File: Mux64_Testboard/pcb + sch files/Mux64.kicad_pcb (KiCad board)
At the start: 4 copper layers, 201.3 x 130.3 mm, 125 parts, among them J1 QTE-020-01-X-D-A, J10 Conn_01x24, J11 Screw_Terminal_01x12, J12 Screw_Terminal_01x06, J13 Screw_Terminal_01x12, J14 Screw_Terminal_01x12, J16 Screw_Terminal_01x12, J17 Screw_Terminal_01x12, J18 Screw_Terminal_01x12, J2 QTE-020-01-X-D-A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

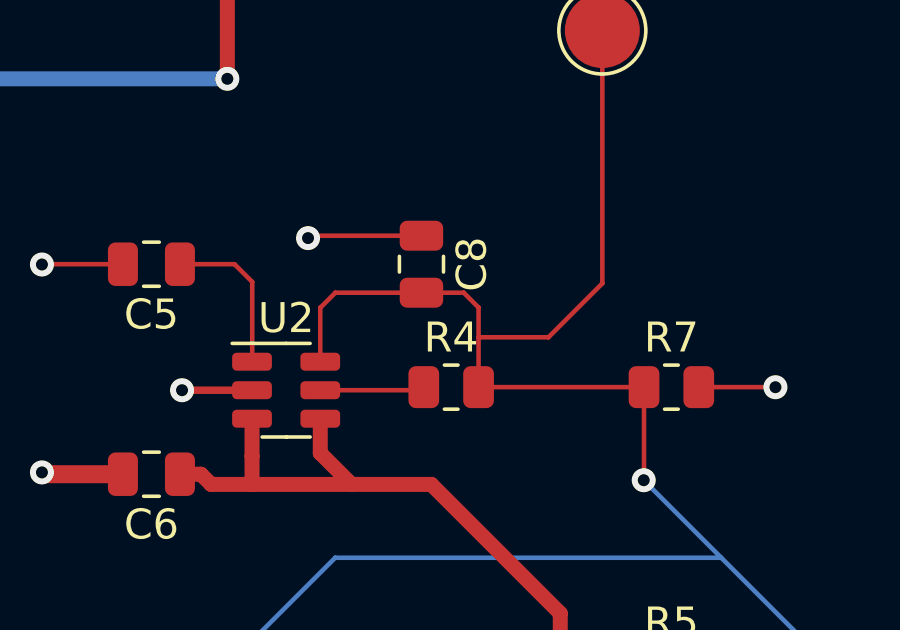
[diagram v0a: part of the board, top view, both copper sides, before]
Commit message: Added images of physical board changes
physical changes from batch order from version 1v0
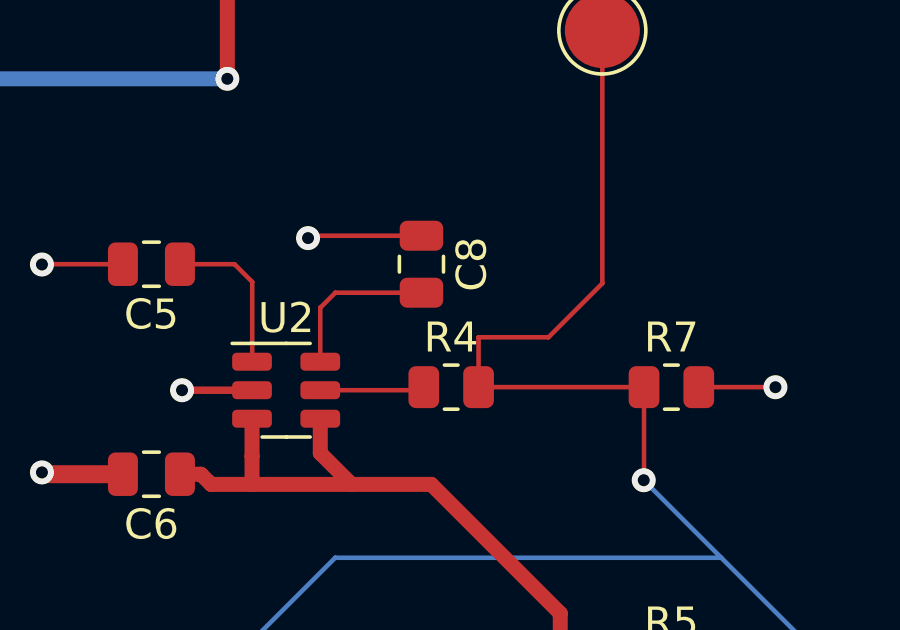
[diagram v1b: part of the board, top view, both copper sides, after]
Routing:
- net B_a4: track 135.9 -> 132.8 mm
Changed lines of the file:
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@@
   (segment (start 186.2239 59.1561) (end 188.5539 59.1561) (width 0.1524) (layer "F.Cu") (net 5))
   (segment (start 188.5539 59.1561) (end 190.35 57.36) (width 0.1524) (layer "F.Cu") (net 5))
-  (segment (start 184.32 57.67) (end 185.73 57.67) (width 0.1524) (layer "F.Cu") (net 5))
-  (segment (start 185.73 57.67) (end 186.2239 58.1639) (width 0.1524) (layer "F.Cu") (net 5))
   (segment (start 231.59 87.29) (end 217.03 72.73) (width 0.1524) (layer "F.Cu") (net 5))
   (segment (start 186.2239 59.1561) (end 186.2239 60.8174) (width 0.1524) (layer "F.Cu") (net 5))
   (segment (start 184.32 57.67) (end 181.45 57.67) (width 0.1524) (layer "F.Cu") (net 5))
-  (segment (start 186.2239 58.1639) (end 186.2239 59.1561) (width 0.1524) (layer "F.Cu") (net 5))
   (segment (start 181.45 57.67) (end 180.9475 58.1725) (width 0.1524) (layer "F.Cu") (net 5))
   (segment (start 237.86 89.63) (end 233.93 89.63) (width 0.1524) (layer "F.Cu") (net 5))

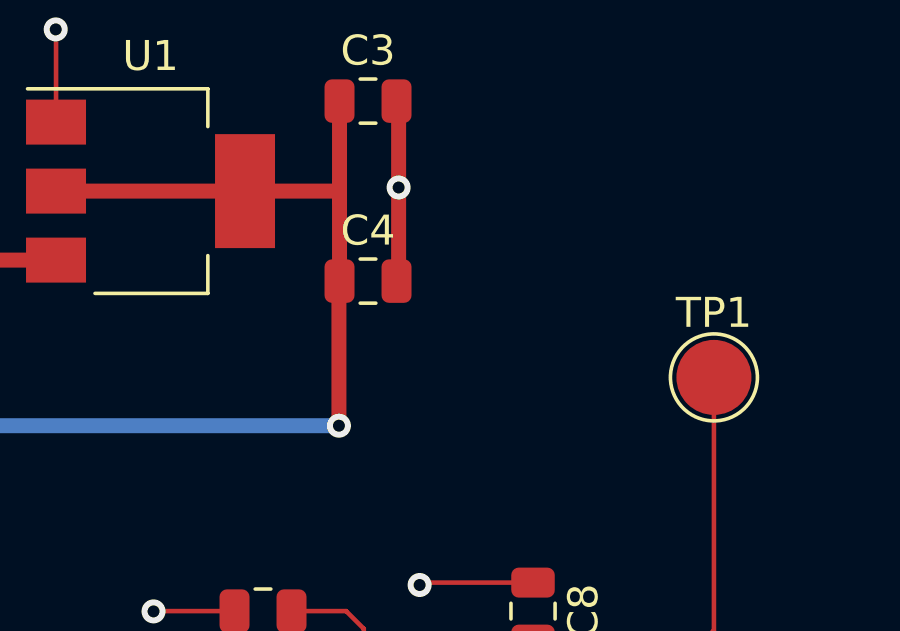
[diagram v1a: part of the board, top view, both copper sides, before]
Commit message: Made improvements on v1.0
Added a 100Ohm load to voltage regulator. Fixed wiring with voltage reference
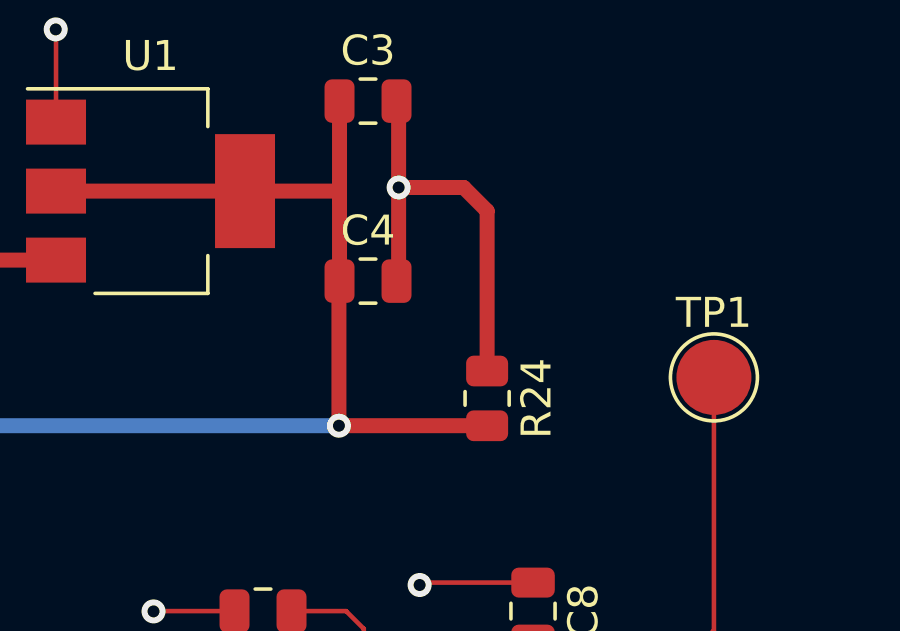
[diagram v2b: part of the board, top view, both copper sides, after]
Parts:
- added R24: 1Kohm, Resistor_SMD:R_0805_2012Metric, F.Cu at (182.8, 49.6)
- C1, C3: value 100nF -> 0.1uF
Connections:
- C8 pad 2: B_a4 -> Net-(R4-Pad1)
- U2 pad 6: B_a4 -> Net-(R4-Pad1)
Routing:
- net MUX64_A11: track 486.3 -> 494.9 mm
- net Net-(R4-Pad1): track 3.49 -> 8.87 mm
- net B_a4: track 132.8 -> 127.4 mm
- net 1.2V: track 138.5 -> 143.4 mm
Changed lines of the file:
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@@
       (effects (font (size 1 1) (thickness 0.15)))
     )
-    (fp_text value "100nF" (at 0 1.68) (layer "F.Fab")
+    (fp_text value "0.1uF" (at 0 1.68) (layer "F.Fab")
       (effects (font (size 1 1) (thickness 0.15)))
     )
@@
       (net 218 "Net-(R4-Pad1)") (pinfunction "OUTS") (pintype "input"))
     (pad "6" smd roundrect (at 1.1375 -0.95) (size 1.325 0.6) (layers "F.Cu" "F.Paste" "F.Mask") (roundrect_rratio 0.25)
-      (net 5 "B_a4") (pinfunction "OUTF") (pintype "input"))
+      (net 218 "Net-(R4-Pad1)") (pinfunction "OUTF") (pintype "input"))
     (model "${KICAD6_3DMODEL_DIR}/Package_TO_SOT_SMD.3dshapes/SOT-23-6.wrl"
       (offset (xyz 0 0 0))
@@
       (effects (font (size 1 1) (thickness 0.15)))
     )
-    (fp_text value "100nF" (at 0 1.68) (layer "F.Fab")
+    (fp_text value "0.1uF" (at 0 1.68) (layer "F.Fab")
       (effects (font (size 1 1) (thickness 0.15)))
     )
@@
       (net 185 "MUX64_A11") (pintype "passive"))
     (pad "2" smd roundrect (at 0.95 0 270) (size 1 1.45) (layers "F.Cu" "F.Paste" "F.Mask") (roundrect_rratio 0.25)
-      (net 5 "B_a4") (pintype "passive"))
+      (net 218 "Net-(R4-Pad1)") (pintype "passive"))
     (model "${KICAD6_3DMODEL_DIR}/Capacitor_SMD.3dshapes/C_0805_2012Metric.wrl"
       (offset (xyz 0 0 0))
@@
   )
   (footprint "Resistor_SMD:R_0805_2012Metric" (layer "F.Cu")
+    (at 182.79 49.63 -90)
+    (descr "Resistor SMD 0805 (2012 Metric), square (rectangular) end terminal, IPC_7351 nominal, (Body size source: IPC-SM-782 page 72, https://www.pcb-3d.com/wordpress/wp-content/uploads/ipc-sm-782a_amendment_1_and_2.pdf), generated with kicad-footprint-generator")
+    (tags "resistor")
+    (property "Sheetfile" "mux64-regulators.kicad_sch")
+    (property "Sheetname" "mux64-regulators")
+    (attr smd)
+    (fp_text reference "R24" (at 0 -1.65 90) (layer "F.SilkS")
+      (effects (font (size 1 1) (thickness 0.15)))
+    )
+    (fp_text value "1Kohm" (at 0 1.65 90) (layer "F.Fab")
+      (effects (font (size 1 1) (thickness 0.15)))
+    )
+    (fp_text user "${REFERENCE}" (at 0 0 90) (layer "F.Fab")
+      (effects (font (size 0.5 0.5) (thickness 0.08)))
+    )
+    (fp_line (start -0.227064 -0.735) (end 0.227064 -0.735) (layer "F.SilkS") (width 0.12))
+    (fp_line (start -0.227064 0.735) (end 0.227064 0.735) (layer "F.SilkS") (width 0.12))
+    (fp_line (start 1.68 0.95) (end -1.68 0.95) (layer "F.CrtYd") (width 0.05))
+    (fp_line (start -1.68 -0.95) (end 1.68 -0.95) (layer "F.CrtYd") (width 0.05))
+    (fp_line (start 1.68 -0.95) (end 1.68 0.95) (layer "F.CrtYd") (width 0.05))
+    (fp_line (start -1.68 0.95) (end -1.68 -0.95) (layer "F.CrtYd") (width 0.05))
+    (fp_line (start 1 0.625) (end -1 0.625) (layer "F.Fab") (width 0.1))
+    (fp_line (start -1 -0.625) (end 1 -0.625) (layer "F.Fab") (width 0.1))
+    (fp_line (start 1 -0.625) (end 1 0.625) (layer "F.Fab") (width 0.1))
+    (fp_line (start -1 0.625) (end -1 -0.625) (layer "F.Fab") (width 0.1))
+    (pad "1" smd roundrect (at -0.9125 0 270) (size 1.025 1.4) (layers "F.Cu" "F.Paste" "F.Mask") (roundrect_rratio 0.243902)
+      (net 185 "MUX64_A11") (pintype "passive"))
+    (pad "2" smd roundrect (at 0.9125 0 270) (size 1.025 1.4) (layers "F.Cu" "F.Paste" "F.Mask") (roundrect_rratio 0.243902)
+      (net 2 "1.2V") (pintype "passive"))
+    (model "${KICAD6_3DMODEL_DIR}/Resistor_SMD.3dshapes/R_0805_2012Metric.wrl"
+      (offset (xyz 0 0 0))
+      (scale (xyz 1 1 1))
+      (rotate (xyz 0 0 0))
+    )
+  )
+  (footprint "Resistor_SMD:R_0805_2012Metric" (layer "F.Cu")
     (at 69.14 66.74 180)
     (descr "Resistor SMD 0805 (2012 Metric), square (rectangular) end terminal, IPC_7351 nominal, (Body size source: IPC-SM-782 page 72, https://www.pcb-3d.com/wordpress/wp-content/uploads/ipc-sm-782a_amendment_1_and_2.pdf), generated with kicad-footprint-generator")
@@
   (segment (start 218.36 126.76) (end 218.36 96.47) (width 0.5) (layer "B.Cu") (net 1))
   (segment (start 177.87 42.79) (end 177.87 42.44) (width 0.5) (layer "F.Cu") (net 2))
+  (segment (start 177.85 50.54) (end 182.7875 50.54) (width 0.5) (layer "F.Cu") (net 2))
   (segment (start 148.61 100.27) (end 155.95 100.27) (width 0.5) (layer "F.Cu") (net 2))
   (segment (start 155.95 100.27) (end 155.995 100.225) (width 0.5) (layer "F.Cu") (net 2))
@@
   (segment (start 158.535 99.545) (end 158.535 96.925) (width 0.5) (layer "F.Cu") (net 2))
   (segment (start 147.2162 96.4838) (end 147.2162 98.8762) (width 0.5) (layer "F.Cu") (net 2))
+  (segment (start 182.7875 50.54) (end 182.79 50.5425) (width 0.5) (layer "F.Cu") (net 2))
   (segment (start 177.85 50.54) (end 177.85 45.74) (width 0.5) (layer "F.Cu") (net 2))
   (segment (start 153.38 91.05) (end 155.9 91.05) (width 0.5) (layer "F.Cu") (net 2))
@@
   (segment (start 231.59 87.29) (end 217.03 72.73) (width 0.1524) (layer "F.Cu") (net 5))
   (segment (start 186.2239 59.1561) (end 186.2239 60.8174) (width 0.1524) (layer "F.Cu") (net 5))
-  (segment (start 184.32 57.67) (end 181.45 57.67) (width 0.1524) (layer "F.Cu") (net 5))
-  (segment (start 181.45 57.67) (end 180.9475 58.1725) (width 0.1524) (layer "F.Cu") (net 5))
   (segment (start 237.86 89.63) (end 233.93 89.63) (width 0.1524) (layer "F.Cu") (net 5))
   (segment (start 233.93 89.63) (end 231.59 87.29) (width 0.1524) (layer "F.Cu") (net 5))
-  (segment (start 180.9475 58.1725) (end 180.9475 59.97) (width 0.1524) (layer "F.Cu") (net 5))
   (segment (start 186.2239 60.8174) (end 191.7395 60.8174) (width 0.1524) (layer "F.Cu") (net 5))
   (segment (start 191.7395 63.9105) (end 191.7395 60.8174) (width 0.1524) (layer "F.Cu") (net 5))
@@
   (segment (start 243.95 137.22) (end 246.2 137.22) (width 0.1524) (layer "F.Cu") (net 185))
   (segment (start 77.97 61.62) (end 80.26 61.62) (width 0.1524) (layer "F.Cu") (net 185))
+  (segment (start 182.79 43.38) (end 182.79 48.7175) (width 0.5) (layer "F.Cu") (net 185))
   (segment (start 111.9525 34.55) (end 114.71 34.55) (width 0.1524) (layer "F.Cu") (net 185))
   (segment (start 244 93.67) (end 246.25 93.67) (width 0.1524) (layer "F.Cu") (net 185))
@@
   (segment (start 207.82 93.67) (end 205.25 93.67) (width 0.1524) (layer "F.Cu") (net 185))
   (segment (start 243.95 132.42) (end 246.07 132.42) (width 0.1524) (layer "F.Cu") (net 185))
+  (segment (start 182.01 42.6) (end 182.79 43.38) (width 0.5) (layer "F.Cu") (net 185))
   (segment (start 210.95 43.255) (end 210.95 37.985) (width 0.1524) (layer "F.Cu") (net 185))
   (segment (start 205.82 50.03) (end 205.77 49.98) (width 0.1524) (layer "F.Cu") (net 185))
@@
   (segment (start 240.91 86.895) (end 240.91 81.625) (width 0.2) (layer "F.Cu") (net 185))
   (segment (start 244.04 52.43) (end 246.27 52.43) (width 0.1524) (layer "F.Cu") (net 185))
+  (segment (start 182.79 48.7175) (end 182.7675 48.7175) (width 0.25) (layer "F.Cu") (net 185))
   (segment (start 240.95 54.875) (end 240.95 58.02) (width 0.1524) (layer "F.Cu") (net 185))
   (segment (start 218.7 84.83) (end 218.88 84.65) (width 0.1524) (layer "F.Cu") (net 185))
@@
   (segment (start 246.19 47.63) (end 246.23 47.67) (width 0.1524) (layer "F.Cu") (net 185))
   (segment (start 205.68 40.43) (end 205.66 40.41) (width 0.1524) (layer "F.Cu") (net 185))
+  (segment (start 179.84 42.6) (end 182.01 42.6) (width 0.5) (layer "F.Cu") (net 185))
   (segment (start 214.04 52.43) (end 210.98 52.43) (width 0.1524) (layer "F.Cu") (net 185))
   (segment (start 80.23 34.71) (end 80.24 34.72) (width 0.1524) (layer "F.Cu") (net 185))
@@
   (segment (start 68.1975 29.63) (end 68.2275 29.6) (width 0.1524) (layer "F.Cu") (net 217))
   (segment (start 61.05 29.63) (end 68.1975 29.63) (width 0.1524) (layer "F.Cu") (net 217))
+  (segment (start 184.32 57.67) (end 181.45 57.67) (width 0.1524) (layer "F.Cu") (net 218))
+  (segment (start 181.45 57.67) (end 180.9475 58.1725) (width 0.1524) (layer "F.Cu") (net 218))
+  (segment (start 180.9475 58.1725) (end 180.9475 59.97) (width 0.1524) (layer "F.Cu") (net 218))
   (segment (start 180.9475 60.92) (end 184.2963 60.92) (width 0.1524) (layer "F.Cu") (net 218))
   (segment (start 184.2963 60.92) (end 184.3989 60.8174) (width 0.1524) (layer "F.Cu") (net 218))

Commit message: Completed v2
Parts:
- moved J1 30.0 mm to (240.9, 133.6)
- moved J2 30.0 mm to (240.9, 46.4)
- moved J3 30.0 mm to (210.9, 133.6)
- moved J4 30.0 mm to (210.9, 46.4)
- moved J5 30.0 mm to (240.9, 90.0)
- moved J6 30.0 mm to (210.9, 90.0)
- moved R1 30.0 mm to (249.2, 137.4)
- moved R2 30.0 mm to (249.2, 50.1)
- moved R3 30.0 mm to (249.2, 93.8)
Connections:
- J9 pad 3: MUX64_A11 -> MUX64_A36
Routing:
- net B_d4: track 119.1 -> 68.9 mm, vias 1 -> 0
- net B_d5: track 119.1 -> 69.1 mm, vias 1 -> 0
- net LV_RB: track 349.7 -> 395.5 mm, vias 5 -> 6
- net B_a4: track 127.4 -> 104.1 mm
- net B_a0(MUX_OUT): track 75.3 -> 86.9 mm, vias 0 -> 2
- net MUX64_A11: track 494.9 -> 484.6 mm
- net B_d0: track 124.5 -> 116.7 mm, vias 0 -> 2
- net B_d3: track 108.1 -> 113.2 mm, vias 0 -> 2
- net Net-(U2-OUTF): track 8.87 -> 12.1 mm
- net B_d1: track 117.0 -> 114.1 mm, vias 0 -> 2
- net MUX64_A35: track 154.2 -> 153.2 mm
- net B_d2: track 115.2 -> 114.3 mm, vias 0 -> 2
